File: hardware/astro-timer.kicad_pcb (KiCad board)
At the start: 2 copper layers, 65.8 x 41.4 mm, 36 parts, among them J1 AVR-ISP-6, J2 AudioJack3, Q1 Q_NPN_BEC, Q2 Q_NPN_BEC, SW1 SW_SPST, SW2 SW_Push, SW3 SW_Push, SW4 Rotary_Encoder_Switch, U1 ATmega328P-AU, Y1 Crystal

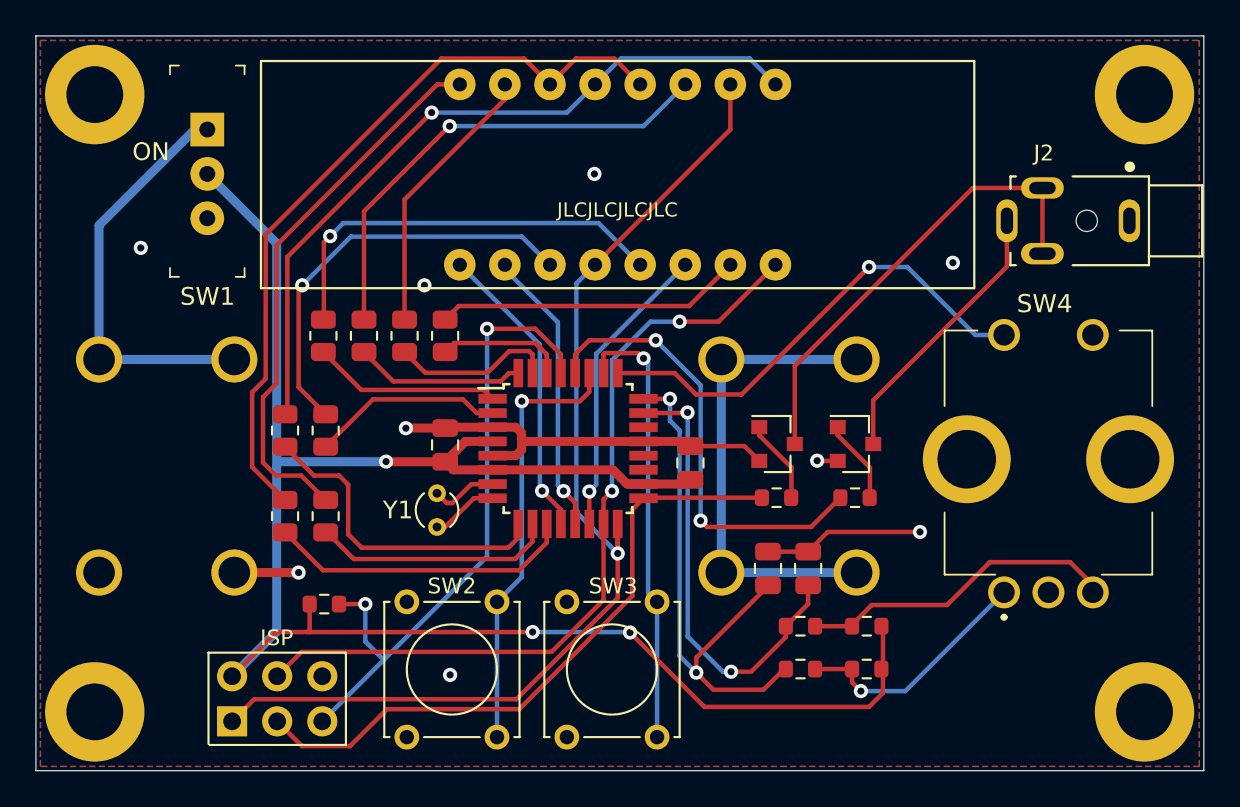
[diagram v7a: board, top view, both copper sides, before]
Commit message: increase ISP header and filter cap clearance
wish I'd noticed these issues before I sent the gerbers to the fab
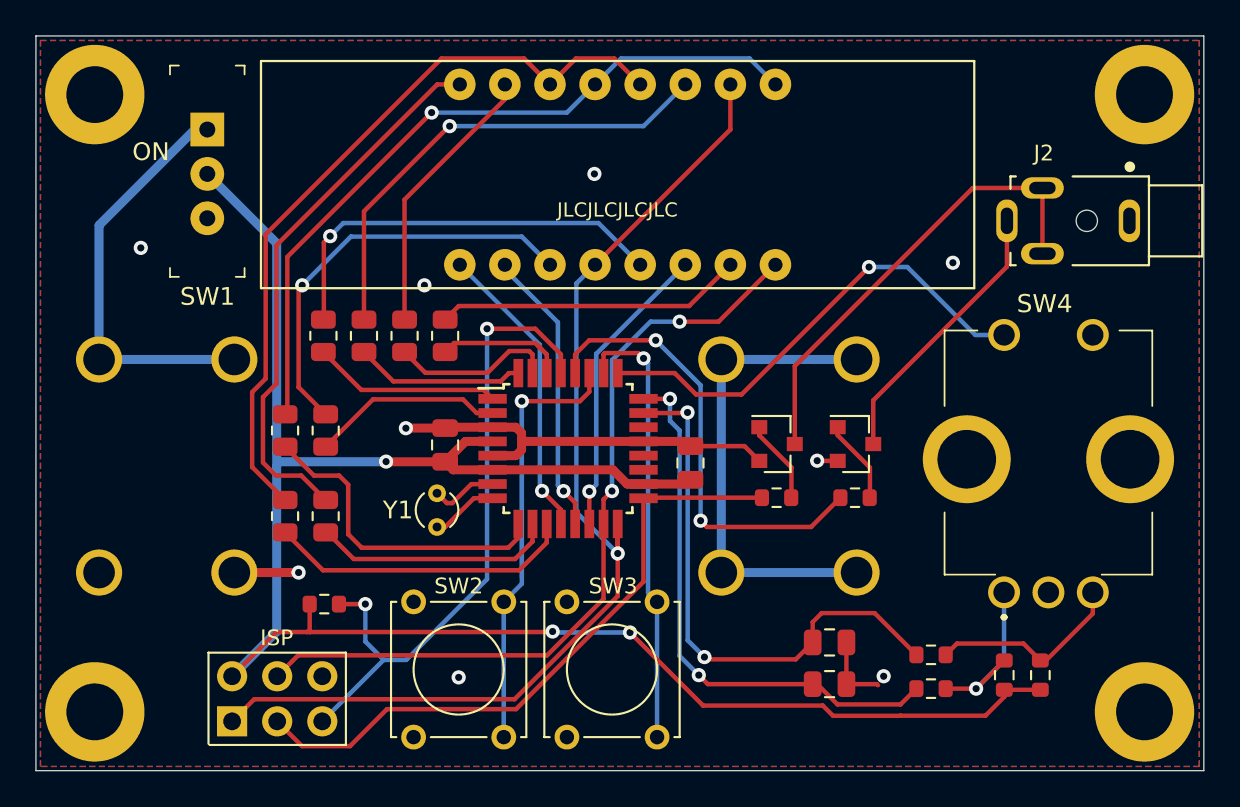
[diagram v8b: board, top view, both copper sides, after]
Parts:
- moved R13 10.2 mm to (139.0, 122.8), turned to 270 degrees
- moved R14 7.75 mm to (137.0, 122.8), turned to 270 degrees
- moved R11 7.53 mm to (132.8, 121.7)
- moved R12 7.44 mm to (132.8, 123.6)
- moved C3 7.38 mm to (127.1, 123.3), turned to 0 degrees
- moved C4 4.34 mm to (127.1, 121.0), turned to 0 degrees
- moved SW2 0.38 mm to (103.7, 126.3)
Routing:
- net Net-(R11-Pad1): track 18.1 -> 11.7 mm
- net VCC: track 103.4 -> 109.4 mm
- net /enc_a: track 25.7 -> 31.4 mm
- net GND: track 37.1 -> 32.3 mm
- net Net-(R12-Pad1): track 13.9 -> 10.0 mm
- net /enc_b: track 30.0 -> 31.4 mm
- net /rst: track 36.8 -> 37.6 mm
